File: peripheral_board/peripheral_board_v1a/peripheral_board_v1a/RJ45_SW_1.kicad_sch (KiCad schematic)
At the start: 7 parts, among them J6 RJ45_Pulse_JXD6-0001NL

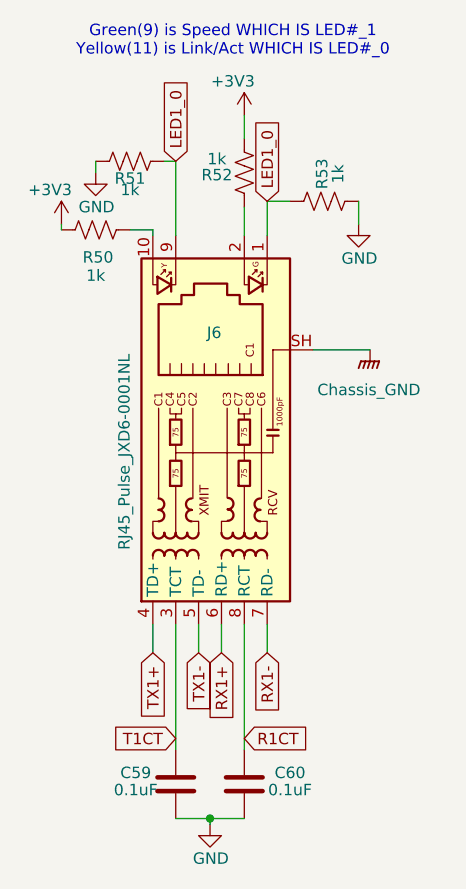
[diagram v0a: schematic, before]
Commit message: PCB Update
Got all the parts on the board placed. Now just finishing the routing for each interconnection.
Trying to maintain a side to side/up to down but the board kinda follows it. For each plane  there is fill zones that will be for the chip that is on the top. Some of the traces are just being fed to where they need to go but the important EMI signals are being contained to their guidelines.
I will need to look at the lengths of the traces to make sure they are kept around the same length.

Will need to go over the board with some other eyes to make sure its ok.

I made sure the Wiznet traces are the same as SALAD.
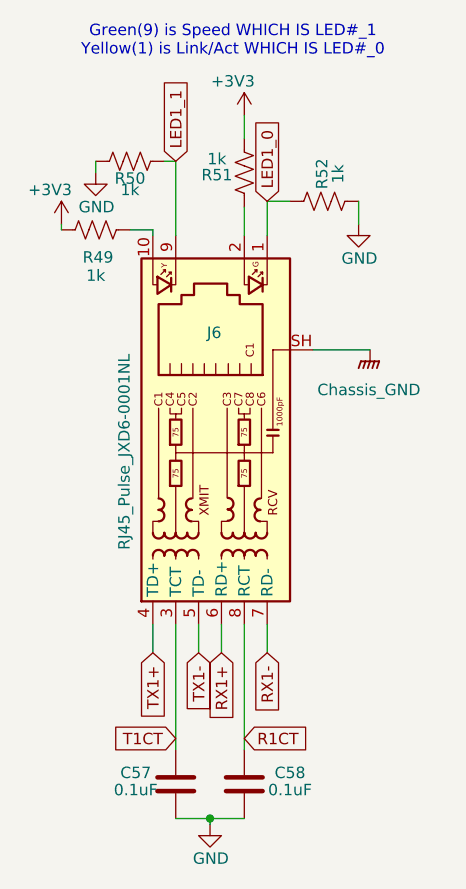
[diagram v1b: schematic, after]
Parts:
- renumbered C59 to C57, C60 to C58, R50 to R49, R51 to R50, R52 to R51, R53 to R52
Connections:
- net LED1_0: no longer J6.9, R50.1
- new net LED1_1: J6.9, R50.1
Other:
- note added: "Green(9) is Speed WHICH IS LED#_1 Yellow(1) is Link/Act WHICH IS LED#_0"
- note removed: "Green(9) is Speed WHICH IS LED#_1 Yellow(11) is Link/Act WHICH IS LED#_0"

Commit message: PCB almost done
Finished the routing except for the power board connector. Will be looking into adding in a Power path controller or similar. Want to add in via stitching for the DP signals. Should be just about done it would be more of just doing some change/improvements.
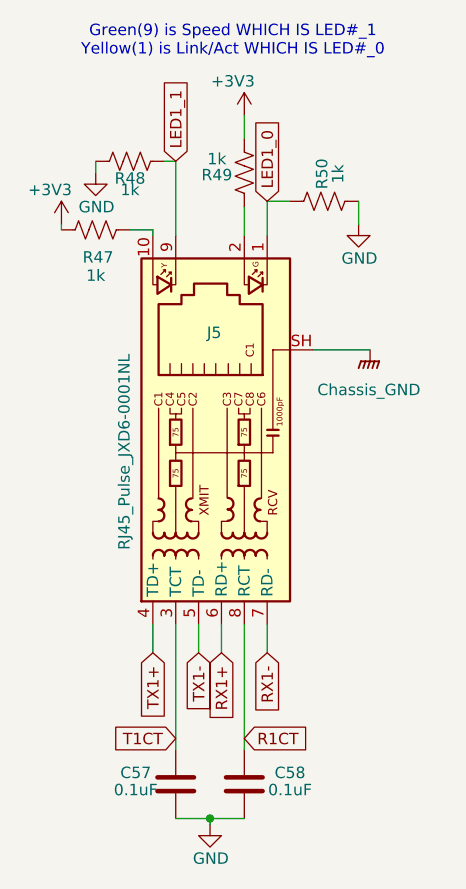
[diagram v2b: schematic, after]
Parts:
- renumbered J6 to J5, R49 to R47, R50 to R48, R51 to R49, R52 to R50
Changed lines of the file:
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@@
 		(on_board yes)
 		(dnp no)
-		(property "Reference" "R49"
+		(property "Reference" "R47"
 			(at 74.549 62.103 90)
 			(effects
@@
 			(project "peripheral_board"
 				(path "/14f8712f-1710-40cb-b01e-cc9b3c4405bd/bdffb641-9271-40a7-b849-e20d9ae38619/32df4f7b-31db-4dfa-a429-7301669e4423"
-					(reference "R49")
+					(reference "R47")
 					(unit 1)
 				)
@@
 		(on_board yes)
 		(dnp no)
-		(property "Reference" "#PWR0138"
+		(property "Reference" "#PWR0134"
 			(at 86.995 131.445 0)
 			(effects
@@
 			(project "peripheral_board"
 				(path "/14f8712f-1710-40cb-b01e-cc9b3c4405bd/bdffb641-9271-40a7-b849-e20d9ae38619/32df4f7b-31db-4dfa-a429-7301669e4423"
-					(reference "#PWR0138")
+					(reference "#PWR0134")
 					(unit 1)
 				)
@@
 		(on_board yes)
 		(dnp no)
-		(property "Reference" "#PWR0136"
+		(property "Reference" "#PWR0132"
 			(at 70.485 62.23 0)
 			(effects
@@
 			(project "peripheral_board"
 				(path "/14f8712f-1710-40cb-b01e-cc9b3c4405bd/bdffb641-9271-40a7-b849-e20d9ae38619/32df4f7b-31db-4dfa-a429-7301669e4423"
-					(reference "#PWR0136")
+					(reference "#PWR0132")
 					(unit 1)
 				)
@@
 		(on_board yes)
 		(dnp no)
-		(property "Reference" "#PWR0140"
+		(property "Reference" "#PWR0136"
 			(at 103.505 64.77 0)
 			(effects
@@
 			(project "peripheral_board"
 				(path "/14f8712f-1710-40cb-b01e-cc9b3c4405bd/bdffb641-9271-40a7-b849-e20d9ae38619/32df4f7b-31db-4dfa-a429-7301669e4423"
-					(reference "#PWR0140")
+					(reference "#PWR0136")
 					(unit 1)
 				)
@@
 		(on_board yes)
 		(dnp no)
-		(property "Reference" "#PWR0137"
+		(property "Reference" "#PWR0133"
 			(at 74.295 59.055 0)
 			(effects
@@
 			(project "peripheral_board"
 				(path "/14f8712f-1710-40cb-b01e-cc9b3c4405bd/bdffb641-9271-40a7-b849-e20d9ae38619/32df4f7b-31db-4dfa-a429-7301669e4423"
-					(reference "#PWR0137")
+					(reference "#PWR0133")
 					(unit 1)
 				)
@@
 		(on_board yes)
 		(dnp no)
-		(property "Reference" "R51"
+		(property "Reference" "R49"
 			(at 87.757 52.959 0)
 			(effects
@@
 			(project "peripheral_board"
 				(path "/14f8712f-1710-40cb-b01e-cc9b3c4405bd/bdffb641-9271-40a7-b849-e20d9ae38619/32df4f7b-31db-4dfa-a429-7301669e4423"
-					(reference "R51")
+					(reference "R49")
 					(unit 1)
 				)
@@
 		(on_board yes)
 		(dnp no)
-		(property "Reference" "#PWR0139"
+		(property "Reference" "#PWR0135"
 			(at 90.805 50.165 0)
 			(effects
@@
 			(project "peripheral_board"
 				(path "/14f8712f-1710-40cb-b01e-cc9b3c4405bd/bdffb641-9271-40a7-b849-e20d9ae38619/32df4f7b-31db-4dfa-a429-7301669e4423"
-					(reference "#PWR0139")
+					(reference "#PWR0135")
 					(unit 1)
 				)
@@
 		(dnp no)
 		(fields_autoplaced yes)
-		(property "Reference" "#PWR0141"
+		(property "Reference" "#PWR0137"
 			(at 104.775 77.47 0)
 			(effects
@@
 			(project "peripheral_board"
 				(path "/14f8712f-1710-40cb-b01e-cc9b3c4405bd/bdffb641-9271-40a7-b849-e20d9ae38619/32df4f7b-31db-4dfa-a429-7301669e4423"
-					(reference "#PWR0141")
+					(reference "#PWR0137")
 					(unit 1)
 				)
@@
 		(on_board yes)
 		(dnp no)
-		(property "Reference" "R50"
+		(property "Reference" "R48"
 			(at 78.105 53.34 90)
 			(effects
@@
 			(project "peripheral_board"
 				(path "/14f8712f-1710-40cb-b01e-cc9b3c4405bd/bdffb641-9271-40a7-b849-e20d9ae38619/32df4f7b-31db-4dfa-a429-7301669e4423"
-					(reference "R50")
+					(reference "R48")
 					(unit 1)
 				)
@@
 		(on_board yes)
 		(dnp no)
-		(property "Reference" "R52"
+		(property "Reference" "R50"
 			(at 99.441 52.832 0)
 			(effects
@@
 			(project "peripheral_board"
 				(path "/14f8712f-1710-40cb-b01e-cc9b3c4405bd/bdffb641-9271-40a7-b849-e20d9ae38619/32df4f7b-31db-4dfa-a429-7301669e4423"
-					(reference "R52")
+					(reference "R50")
 					(unit 1)
 				)
@@
 		(on_board yes)
 		(dnp no)
-		(property "Reference" "J6"
+		(property "Reference" "J5"
 			(at 88.265 70.485 90)
 			(effects
@@
 			(project ""
 				(path "/14f8712f-1710-40cb-b01e-cc9b3c4405bd/bdffb641-9271-40a7-b849-e20d9ae38619/32df4f7b-31db-4dfa-a429-7301669e4423"
-					(reference "J6")
-					(unit 1)
-				)
+					(reference "J5")
+					(unit 1)
+				)

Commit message: Part picking for board
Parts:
- C57, C58: value 0.1uF -> 100nF
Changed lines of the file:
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@@
 			)
 		)
-		(property "Value" "0.1uF"
+		(property "Value" "100nF"
 			(at 95.885 121.285 0)
 			(effects
@@
 			)
 		)
-		(property "Value" "0.1uF"
-			(at 78.74 121.285 0)
+		(property "Value" "100nF"
+			(at 76.835 121.285 0)
 			(effects
 				(font

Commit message: PCB step update
Made some additions to the 3d files for the project.
Deleted some old files that were just not being used.
Would like to restructure the folders and remove the v1 and make a folder that is just KiCad dependancies to help version control.
*Unsure if that is a good idea or if I should just leave it as project specific libriaries.*
Will look over this before this is merged to main.
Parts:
- renumbered C58 to C?, C57 to C?, J5 to J?, R47 to R?, R49 to R?, R48 to R?, R50 to R?
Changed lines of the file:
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@@
 		(on_board yes)
 		(dnp no)
-		(property "Reference" "R47"
+		(property "Reference" "R?"
 			(at 74.549 62.103 90)
 			(effects
@@
 		)
 		(instances
-			(project "peripheral_board"
-				(path "/14f8712f-1710-40cb-b01e-cc9b3c4405bd/bdffb641-9271-40a7-b849-e20d9ae38619/32df4f7b-31db-4dfa-a429-7301669e4423"
-					(reference "R47")
+			(project "peripheral_board_v1a"
+				(path "/14f8712f-1710-40cb-b01e-cc9b3c4405bd/bdffb641-9271-40a7-b849-e20d9ae38619/32df4f7b-31db-4dfa-a429-7301669e4423"
+					(reference "R?")
 					(unit 1)
 				)
@@
 		(on_board yes)
 		(dnp no)
-		(property "Reference" "#PWR0134"
+		(property "Reference" "#PWR?"
 			(at 86.995 131.445 0)
 			(effects
@@
 		)
 		(instances
-			(project "peripheral_board"
-				(path "/14f8712f-1710-40cb-b01e-cc9b3c4405bd/bdffb641-9271-40a7-b849-e20d9ae38619/32df4f7b-31db-4dfa-a429-7301669e4423"
-					(reference "#PWR0134")
+			(project "peripheral_board_v1a"
+				(path "/14f8712f-1710-40cb-b01e-cc9b3c4405bd/bdffb641-9271-40a7-b849-e20d9ae38619/32df4f7b-31db-4dfa-a429-7301669e4423"
+					(reference "#PWR?")
 					(unit 1)
 				)
@@
 		(on_board yes)
 		(dnp no)
-		(property "Reference" "C58"
+		(property "Reference" "C?"
 			(at 95.885 119.38 0)
 			(effects
@@
 		)
 		(instances
-			(project "peripheral_board"
-				(path "/14f8712f-1710-40cb-b01e-cc9b3c4405bd/bdffb641-9271-40a7-b849-e20d9ae38619/32df4f7b-31db-4dfa-a429-7301669e4423"
-					(reference "C58")
+			(project "peripheral_board_v1a"
+				(path "/14f8712f-1710-40cb-b01e-cc9b3c4405bd/bdffb641-9271-40a7-b849-e20d9ae38619/32df4f7b-31db-4dfa-a429-7301669e4423"
+					(reference "C?")
 					(unit 1)
 				)
@@
 		(on_board yes)
 		(dnp no)
-		(property "Reference" "#PWR0132"
+		(property "Reference" "#PWR?"
 			(at 70.485 62.23 0)
 			(effects
@@
 		)
 		(instances
-			(project "peripheral_board"
-				(path "/14f8712f-1710-40cb-b01e-cc9b3c4405bd/bdffb641-9271-40a7-b849-e20d9ae38619/32df4f7b-31db-4dfa-a429-7301669e4423"
-					(reference "#PWR0132")
+			(project "peripheral_board_v1a"
+				(path "/14f8712f-1710-40cb-b01e-cc9b3c4405bd/bdffb641-9271-40a7-b849-e20d9ae38619/32df4f7b-31db-4dfa-a429-7301669e4423"
+					(reference "#PWR?")
 					(unit 1)
 				)
@@
 		(on_board yes)
 		(dnp no)
-		(property "Reference" "C57"
+		(property "Reference" "C?"
 			(at 78.74 119.38 0)
 			(effects
@@
 		)
 		(instances
-			(project "peripheral_board"
-				(path "/14f8712f-1710-40cb-b01e-cc9b3c4405bd/bdffb641-9271-40a7-b849-e20d9ae38619/32df4f7b-31db-4dfa-a429-7301669e4423"
-					(reference "C57")
+			(project "peripheral_board_v1a"
+				(path "/14f8712f-1710-40cb-b01e-cc9b3c4405bd/bdffb641-9271-40a7-b849-e20d9ae38619/32df4f7b-31db-4dfa-a429-7301669e4423"
+					(reference "C?")
 					(unit 1)
 				)
@@
 		(on_board yes)
 		(dnp no)
-		(property "Reference" "#PWR0136"
+		(property "Reference" "#PWR?"
 			(at 103.505 64.77 0)
 			(effects
@@
 		)
 		(instances
-			(project "peripheral_board"
-				(path "/14f8712f-1710-40cb-b01e-cc9b3c4405bd/bdffb641-9271-40a7-b849-e20d9ae38619/32df4f7b-31db-4dfa-a429-7301669e4423"
-					(reference "#PWR0136")
+			(project "peripheral_board_v1a"
+				(path "/14f8712f-1710-40cb-b01e-cc9b3c4405bd/bdffb641-9271-40a7-b849-e20d9ae38619/32df4f7b-31db-4dfa-a429-7301669e4423"
+					(reference "#PWR?")
 					(unit 1)
 				)
@@
 		(on_board yes)
 		(dnp no)
-		(property "Reference" "#PWR0133"
+		(property "Reference" "#PWR?"
 			(at 74.295 59.055 0)
 			(effects
@@
 		)
 		(instances
-			(project "peripheral_board"
-				(path "/14f8712f-1710-40cb-b01e-cc9b3c4405bd/bdffb641-9271-40a7-b849-e20d9ae38619/32df4f7b-31db-4dfa-a429-7301669e4423"
-					(reference "#PWR0133")
+			(project "peripheral_board_v1a"
+				(path "/14f8712f-1710-40cb-b01e-cc9b3c4405bd/bdffb641-9271-40a7-b849-e20d9ae38619/32df4f7b-31db-4dfa-a429-7301669e4423"
+					(reference "#PWR?")
 					(unit 1)
 				)
@@
 		(on_board yes)
 		(dnp no)
-		(property "Reference" "R49"
+		(property "Reference" "R?"
 			(at 87.757 52.959 0)
 			(effects
@@
 		)
 		(instances
-			(project "peripheral_board"
-				(path "/14f8712f-1710-40cb-b01e-cc9b3c4405bd/bdffb641-9271-40a7-b849-e20d9ae38619/32df4f7b-31db-4dfa-a429-7301669e4423"
-					(reference "R49")
+			(project "peripheral_board_v1a"
+				(path "/14f8712f-1710-40cb-b01e-cc9b3c4405bd/bdffb641-9271-40a7-b849-e20d9ae38619/32df4f7b-31db-4dfa-a429-7301669e4423"
+					(reference "R?")
 					(unit 1)
 				)
@@
 		(on_board yes)
 		(dnp no)
-		(property "Reference" "#PWR0135"
+		(property "Reference" "#PWR?"
 			(at 90.805 50.165 0)
 			(effects
@@
 		)
 		(instances
-			(project "peripheral_board"
-				(path "/14f8712f-1710-40cb-b01e-cc9b3c4405bd/bdffb641-9271-40a7-b849-e20d9ae38619/32df4f7b-31db-4dfa-a429-7301669e4423"
-					(reference "#PWR0135")
+			(project "peripheral_board_v1a"
+				(path "/14f8712f-1710-40cb-b01e-cc9b3c4405bd/bdffb641-9271-40a7-b849-e20d9ae38619/32df4f7b-31db-4dfa-a429-7301669e4423"
+					(reference "#PWR?")
 					(unit 1)
 				)
@@
 		(dnp no)
 		(fields_autoplaced yes)
-		(property "Reference" "#PWR0137"
+		(property "Reference" "#PWR?"
 			(at 104.775 77.47 0)
 			(effects
@@
 		)
 		(instances
-			(project "peripheral_board"
-				(path "/14f8712f-1710-40cb-b01e-cc9b3c4405bd/bdffb641-9271-40a7-b849-e20d9ae38619/32df4f7b-31db-4dfa-a429-7301669e4423"
-					(reference "#PWR0137")
+			(project "peripheral_board_v1a"
+				(path "/14f8712f-1710-40cb-b01e-cc9b3c4405bd/bdffb641-9271-40a7-b849-e20d9ae38619/32df4f7b-31db-4dfa-a429-7301669e4423"
+					(reference "#PWR?")
 					(unit 1)
 				)
@@
 		(on_board yes)
 		(dnp no)
-		(property "Reference" "R48"
+		(property "Reference" "R?"
 			(at 78.105 53.34 90)
 			(effects
@@
 		)
 		(instances
-			(project "peripheral_board"
-				(path "/14f8712f-1710-40cb-b01e-cc9b3c4405bd/bdffb641-9271-40a7-b849-e20d9ae38619/32df4f7b-31db-4dfa-a429-7301669e4423"
-					(reference "R48")
+			(project "peripheral_board_v1a"
+				(path "/14f8712f-1710-40cb-b01e-cc9b3c4405bd/bdffb641-9271-40a7-b849-e20d9ae38619/32df4f7b-31db-4dfa-a429-7301669e4423"
+					(reference "R?")
 					(unit 1)
 				)
@@
 		(on_board yes)
 		(dnp no)
-		(property "Reference" "R50"
+		(property "Reference" "R?"
 			(at 99.441 52.832 0)
 			(effects
@@
 		)
 		(instances
-			(project "peripheral_board"
-				(path "/14f8712f-1710-40cb-b01e-cc9b3c4405bd/bdffb641-9271-40a7-b849-e20d9ae38619/32df4f7b-31db-4dfa-a429-7301669e4423"
-					(reference "R50")
+			(project "peripheral_board_v1a"
+				(path "/14f8712f-1710-40cb-b01e-cc9b3c4405bd/bdffb641-9271-40a7-b849-e20d9ae38619/32df4f7b-31db-4dfa-a429-7301669e4423"
+					(reference "R?")
 					(unit 1)
 				)
@@
 		(on_board yes)
 		(dnp no)
-		(property "Reference" "J5"
+		(property "Reference" "J?"
 			(at 88.265 70.485 90)
 			(effects
@@
 		)
 		(instances
-			(project ""
-				(path "/14f8712f-1710-40cb-b01e-cc9b3c4405bd/bdffb641-9271-40a7-b849-e20d9ae38619/32df4f7b-31db-4dfa-a429-7301669e4423"
-					(reference "J5")
-					(unit 1)
-				)
+			(project "peripheral_board_v1a"
+				(path "/14f8712f-1710-40cb-b01e-cc9b3c4405bd/bdffb641-9271-40a7-b849-e20d9ae38619/32df4f7b-31db-4dfa-a429-7301669e4423"
+					(reference "J?")
+					(unit 1)
+				)
